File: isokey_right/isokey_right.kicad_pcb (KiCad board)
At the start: 2 copper layers, 97.3 x 118.3 mm, 165 parts, among them SW1 Cherry, SW10 Cherry, SW11 Cherry, SW12 Cherry, SW13 Cherry, SW14 Cherry, SW15 Cherry, SW16 Cherry, SW17 Cherry, SW18 Cherry, SW2 Cherry, SW21 Cherry, SW22 Cherry, SW23 Cherry, SW24 Cherry, SW27 Cherry, SW28 Cherry, SW3 Cherry, SW31 Cherry, SW32 Cherry, SW33 Cherry, SW34 Cherry, SW37 Cherry, SW38 Cherry, SW4 Cherry, SW41 Cherry, SW42 Cherry, SW43 Cherry, SW44 Cherry, SW5 Cherry, SW6 Cherry, SW9 Cherry

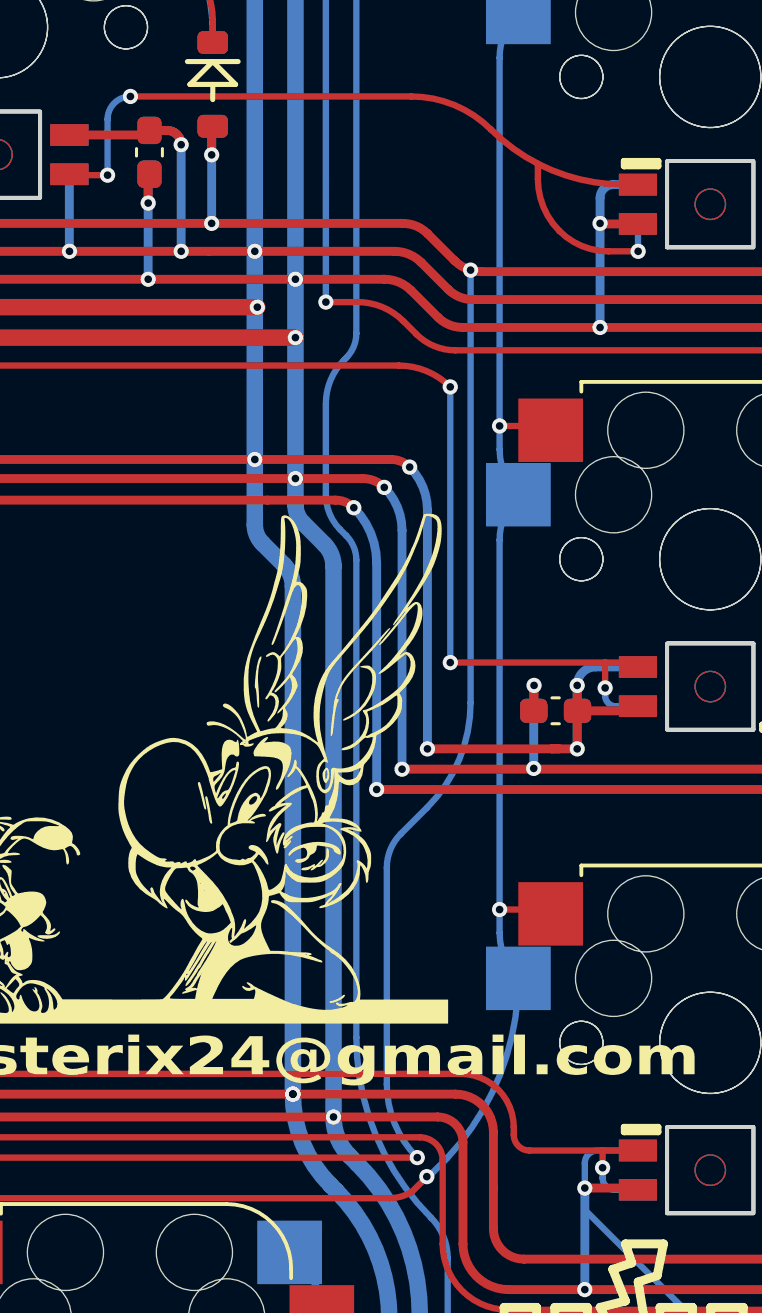
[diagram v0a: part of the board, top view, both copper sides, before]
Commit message: add frame pcb
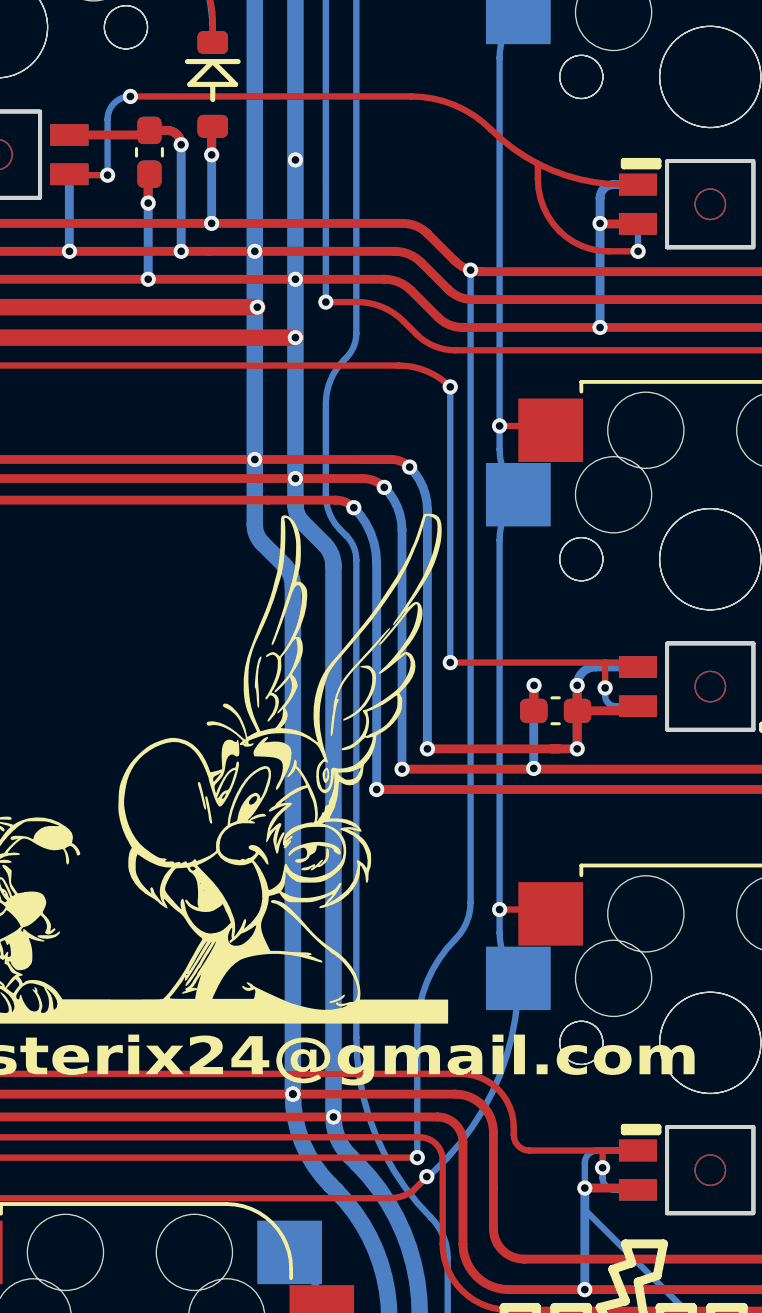
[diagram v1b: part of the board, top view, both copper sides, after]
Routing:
- net /r1: track 223.3 -> 222.6 mm
- net GND: vias 80 -> 81
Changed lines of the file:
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@@
   (gr_circle (center 93.00025 142.098914) (end 94.50025 142.098914)
     (stroke (width 0.25) (type solid)) (fill none) (layer "F.Cu"))
-  (gr_rect (start 171.25 132.281263) (end 172.531263 131)
+  (gr_rect (start 171.25 131) (end 172.531263 132.281263)
     (stroke (width 0.35) (type default)) (fill none) (layer "B.SilkS"))
-  (gr_rect (start 175.390631 130.281263) (end 176.671894 129)
+  (gr_rect (start 175.390631 129) (end 176.671894 130.281263)
     (stroke (width 0.35) (type default)) (fill none) (layer "B.SilkS"))
   (gr_line (start 173.140631 129.5) (end 173.890631 129.75)
@@
   (gr_line (start 173.390631 128) (end 173.140631 129.5)
     (stroke (width 0.35) (type default)) (layer "B.SilkS"))
-  (gr_rect (start 171.25 130.281263) (end 172.531263 129)
+  (gr_rect (start 171.25 129) (end 172.531263 130.281263)
     (stroke (width 0.35) (type default)) (fill none) (layer "B.SilkS"))
   (gr_line (start 174.390631 127.5) (end 173.890631 128.75)
     (stroke (width 0.35) (type default)) (layer "B.SilkS"))
-  (gr_rect (start 177.390631 132.281263) (end 178.671894 131)
+  (gr_rect (start 177.390631 131) (end 178.671894 132.281263)
     (stroke (width 0.35) (type default)) (fill none) (layer "B.SilkS"))
   (gr_line (start 173.890631 126.5) (end 173.640631 127.25)
     (stroke (width 0.35) (type default)) (layer "B.SilkS"))
-  (gr_rect (start 175.390631 132.281263) (end 176.671894 131)
+  (gr_rect (start 175.390631 131) (end 176.671894 132.281263)
     (stroke (width 0.35) (type default)) (fill none) (layer "B.SilkS"))
   (gr_line (start 173.890631 128.75) (end 174.890631 129)
@@
   (gr_line (start 173.640631 127.25) (end 174.390631 127.5)
     (stroke (width 0.35) (type default)) (layer "B.SilkS"))
-  (gr_rect (start 169.25 132.281263) (end 170.531263 131)
+  (gr_rect (start 169.25 131) (end 170.531263 132.281263)
     (stroke (width 0.35) (type default)) (fill none) (layer "B.SilkS"))
-  (gr_rect (start 177.390631 130.281263) (end 178.671894 129)
+  (gr_rect (start 177.390631 129) (end 178.671894 130.281263)
     (stroke (width 0.35) (type default)) (fill none) (layer "B.SilkS"))
   (gr_line (start 173.890631 129.75) (end 173.640631 131.5)
@@
   (gr_line (start 174.890631 129) (end 173.640631 131.5)
     (stroke (width 0.35) (type default)) (layer "B.SilkS"))
-  (gr_rect (start 169.25 130.281263) (end 170.531263 129)
+  (gr_rect (start 169.25 129) (end 170.531263 130.281263)
     (stroke (width 0.35) (type default)) (fill none) (layer "B.SilkS"))
-  (gr_rect (start 168.5 130.281263) (end 167.218737 129)
+  (gr_rect (start 167.218737 129) (end 168.5 130.281263)
     (stroke (width 0.35) (type default)) (fill none) (layer "F.SilkS"))
   (gr_line (start 170.25 131.5) (end 170 129.75)
@@
   (gr_rect (start 171.359368 131) (end 172.640631 132.281263)
     (stroke (width 0.35) (type default)) (fill none) (layer "F.SilkS"))
-  (gr_rect (start 168.5 132.281263) (end 167.218737 131)
+  (gr_rect (start 167.218737 131) (end 168.5 132.281263)
     (stroke (width 0.35) (type default)) (fill none) (layer "F.SilkS"))
-  (gr_rect (start 166.5 130.281263) (end 165.218737 129)
+  (gr_rect (start 165.218737 129) (end 166.5 130.281263)
     (stroke (width 0.35) (type default)) (fill none) (layer "F.SilkS"))
   (gr_arc (start 175.35937 131.701117) (mid 178.222362 138.612995) (end 171.310485 135.750001)
@@
   (gr_line (start 170 128.75) (end 169.5 127.5)
     (stroke (width 0.35) (type default)) (layer "F.SilkS"))
-  (gr_rect (start 166.5 132.281263) (end 165.218737 131)
+  (gr_rect (start 165.218737 131) (end 166.5 132.281263)
     (stroke (width 0.35) (type default)) (fill none) (layer "F.SilkS"))
   (gr_rect (start 171.359368 129) (end 172.640631 130.281263)
@@
   (gr_text "K" (at 170.140631 137.75) (layer "B.SilkS")
     (effects (font (face "Courier New") (size 4.5 4.5) (thickness 0.6) bold) (justify left bottom mirror))
-    (render_cache "K" -0
+    (render_cache "K" 0
       (polygon
         (pts
@@
   (gr_text "asterix24@gmail.com" (at 163.5 120) (layer "B.SilkS")
     (effects (font (face "3270 Nerd Font Mono") (size 1.5 1.8) (thickness 0.2) bold) (justify left bottom mirror))
-    (render_cache "asterix24@gmail.com" -0
+    (render_cache "asterix24@gmail.com" 0
       (polygon
         (pts
@@
   (gr_text "iso" (at 175.390631 135) (layer "B.SilkS")
     (effects (font (face "Courier New") (size 2 2) (thickness 0.5) bold) (justify left bottom mirror))
-    (render_cache "iso" -0
+    (render_cache "iso" 0
       (polygon
         (pts
@@
   (via (at 131.6 61.5) (size 0.6) (drill 0.3) (layers "F.Cu" "B.Cu") (net 2))
   (via (at 113.3 78.3) (size 0.6) (drill 0.3) (layers "F.Cu" "B.Cu") (net 2))
+  (via (at 157 83.8) (size 0.6) (drill 0.3) (layers "F.Cu" "B.Cu") (net 2))
   (via (at 151.2 85.5) (size 0.6) (drill 0.3) (layers "F.Cu" "B.Cu") (net 2))
   (via (at 104.7 58.25) (size 0.6) (drill 0.3) (layers "F.Cu" "B.Cu") (net 2))
@@
   (arc (start 135.6 84.7) (mid 136.068629 85.831371) (end 137.2 86.3) (width 0.35) (layer "F.Cu") (net 14))
   (arc (start 94.492894 132.5) (mid 95.146175 132.370054) (end 95.7 132) (width 0.25) (layer "F.Cu") (net 14))
+  (segment (start 163.9 88.140552) (end 163.9 113.051472) (width 0.25) (layer "B.Cu") (net 14))
   (segment (start 153.7 82.51915) (end 153.7 83.6) (width 0.35) (layer "B.Cu") (net 14))
   (segment (start 108.5 74.05015) (end 108.5 72.95015) (width 0.25) (layer "B.Cu") (net 14))
@@
   (segment (start 181.843 85.52975) (end 181.843 84.42975) (width 0.25) (layer "B.Cu") (net 14))
   (segment (start 101.3 131.3) (end 101.3 118.9) (width 0.25) (layer "B.Cu") (net 14))
-  (segment (start 160.6 120.202944) (end 160.6 111.677817) (width 0.25) (layer "B.Cu") (net 14))
-  (segment (start 163.9 105.182803) (end 163.9 88.140552) (width 0.25) (layer "B.Cu") (net 14))
-  (segment (start 161.15 110.35) (end 162.190783 109.309217) (width 0.25) (layer "B.Cu") (net 14))
+  (segment (start 161.8 118.12132) (end 161.8 123.1) (width 0.25) (layer "B.Cu") (net 14))
   (segment (start 127.55 74.05015) (end 127.55 76.55) (width 0.35) (layer "B.Cu") (net 14))
   (segment (start 182.3 86.633045) (end 182.3 88.2) (width 0.25) (layer "B.Cu") (net 14))
@@
   (arc (start 181.843 85.52975) (mid 182.181229 86.035945) (end 182.3 86.633045) (width 0.25) (layer "B.Cu") (net 14))
   (arc (start 127.55 76.55) (mid 127.564645 76.585355) (end 127.6 76.6) (width 0.35) (layer "B.Cu") (net 14))
-  (arc (start 160.6 111.677817) (mid 160.74294 110.959208) (end 161.15 110.35) (width 0.25) (layer "B.Cu") (net 14))
+  (arc (start 163.9 113.051472) (mid 163.744065 113.835409) (end 163.3 114.5) (width 0.25) (layer "B.Cu") (net 14))
   (arc (start 153.744 82.47515) (mid 153.712887 82.488037) (end 153.7 82.51915) (width 0.35) (layer "B.Cu") (net 14))
-  (arc (start 162.190783 109.309217) (mid 163.455789 107.416002) (end 163.9 105.182803) (width 0.25) (layer "B.Cu") (net 14))
-  (arc (start 161.8 123.1) (mid 160.91187 121.77082) (end 160.6 120.202944) (width 0.25) (layer "B.Cu") (net 14))
+  (arc (start 163.3 114.5) (mid 162.189837 116.161475) (end 161.8 118.12132) (width 0.25) (layer "B.Cu") (net 14))
   (segment (start 108.5 69.65015) (end 108.5 68.77951) (width 0.25) (layer "F.Cu") (net 15))
   (arc (start 108.5 68.77951) (mid 108.255702 67.551341) (end 107.56 66.51015) (width 0.25) (layer "F.Cu") (net 15))
